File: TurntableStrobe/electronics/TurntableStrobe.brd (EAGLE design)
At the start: 25.1 x 17.8 mm, 16 parts, among them IC1 TINY25, J1 ISP, Q1 12MHz

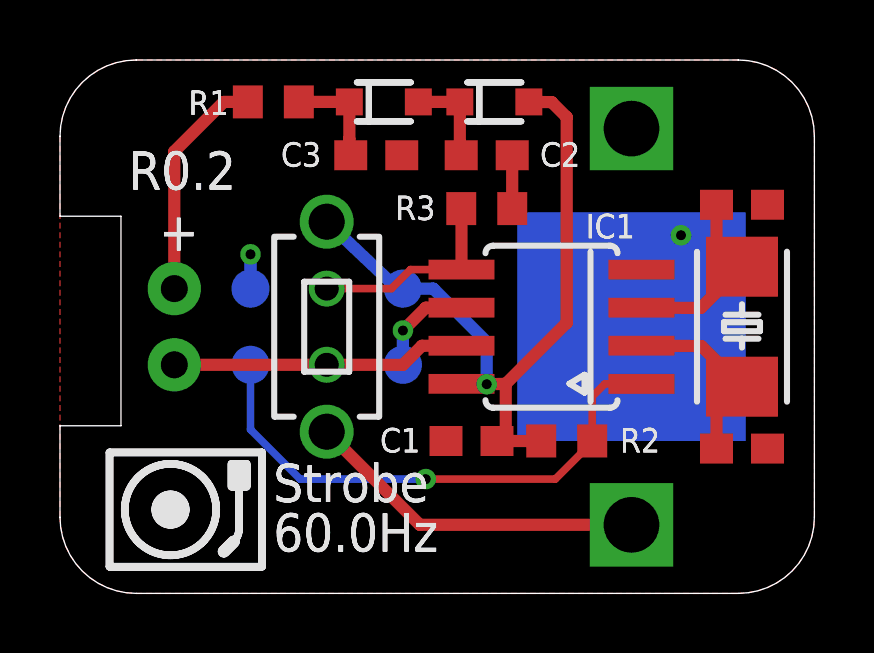
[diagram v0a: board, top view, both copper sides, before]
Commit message: Removed hardware directory. Updated boards. Modified timing calcs spreadsheet.
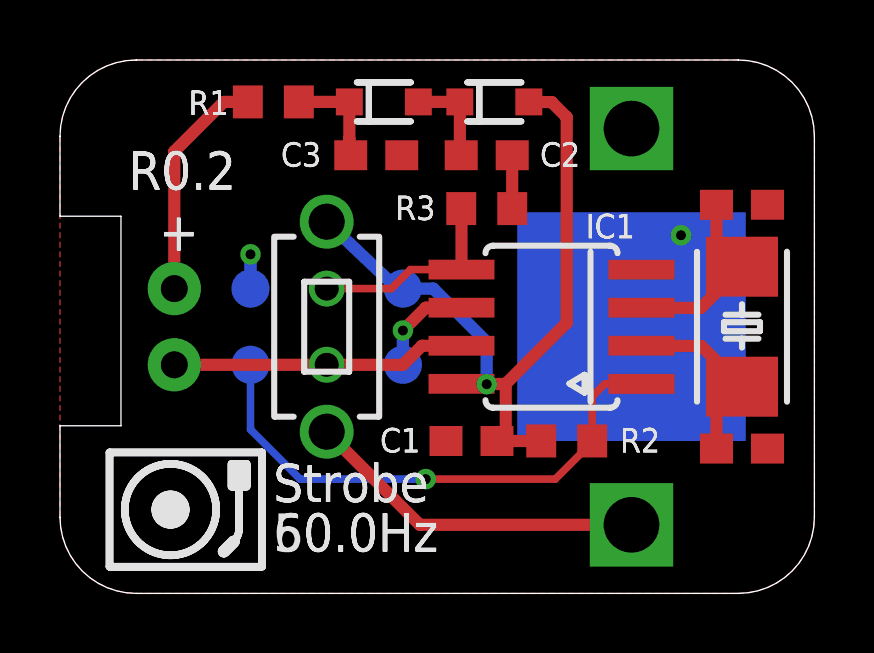
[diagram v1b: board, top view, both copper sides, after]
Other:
- board text added: "50.0Hz"
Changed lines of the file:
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@@
 <text x="7.112" y="3.048" size="1.27" layer="121" font="vector" ratio="16">Strobe</text>
 <text x="2.286" y="13.462" size="1.27" layer="121" font="vector" ratio="16">R0.2</text>
-<text x="7.112" y="1.397" size="1.27" layer="121" font="vector" ratio="16">60.0Hz</text>
+<text x="7.112" y="1.397" size="1.27" layer="121" font="vector" ratio="16">50.0Hz</text>
 <text x="10.668" y="4.699" size="0.8128" layer="121" font="vector" ratio="25">C1</text>
 <text x="16.002" y="14.224" size="0.8128" layer="121" font="vector" ratio="25">C2</text>
